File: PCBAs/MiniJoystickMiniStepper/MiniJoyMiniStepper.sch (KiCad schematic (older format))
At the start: 72 parts, among them J0 STEPPER_UNI_5P, J1 STEPPER_UNI_5P, J10 TH_0.1_1x1, J100 TH_0.1_1x1, J101 TH_0.1_1x1, J102 TH_0.1_1x1, J103 TH_0.1_1x1, J104 TH_0.1_1x1, J105 TH_0.1_1x1, J107 TH_0.1_1x1, J11 TH_0.1_1x1, J12 TH_0.1_1x1, J13 TH_0.1_1x1, J14 TH_0.1_1x1, J15 TH_0.1_1x1, J16 TH_0.1_1x1, J2 STEPPER_UNI_5P, J3 STEPPER_UNI_5P, J4 STEPPER_UNI_5P, J5 STEPPER_UNI_5P, J6 STEPPER_UNI_5P, J7 STEPPER_UNI_5P, J8 TH_0.1_1x1, J9 TH_0.1_1x1, U1 MCP3008T-I/SL, U10 ULN2803, U11 STM32F103C8T6_BLUE_PILL, U2 OLED_128x32_I2C, U3 CD74HC595, U4 CD74HC595, U5 CD74HC595, U6 CD74HC595, U7 ULN2803, U8 ULN2803, U9 ULN2803

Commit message: Updated daisy chain con, added motor power and xtra gnd
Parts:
- added JMOTOR_GND11, JMOTOR_GND3, J_MOTOR_POWER0, J_MOTOR_POWER1: TH_0.1_1x1, Liberry:single_0.1, symbol TH_0.1_1x1
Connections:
- wire segments 416 -> 423
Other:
- moved on the sheet: C1, J101, J102, J103, J104, J105, J107, J11, J12, J13, J14, J15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

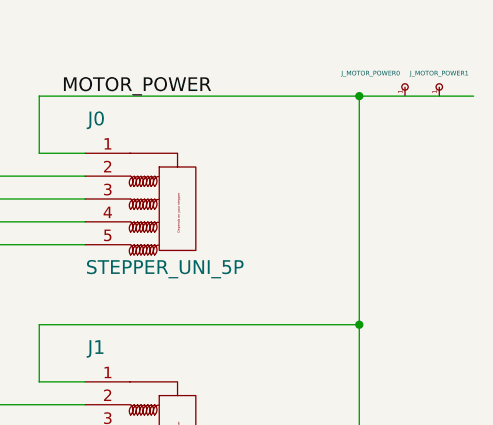
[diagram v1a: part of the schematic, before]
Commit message: Updated daisy chain. Added extra motor power pins for more current/heat disspation.
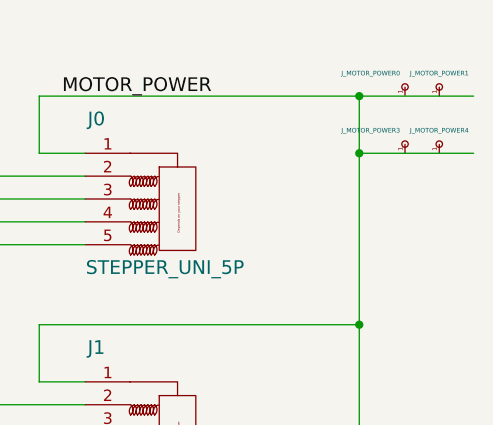
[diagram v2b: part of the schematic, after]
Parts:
- added J_MOTOR_POWER3, J_MOTOR_POWER4: TH_0.1_1x1, Liberry:single_0.1, symbol TH_0.1_1x1
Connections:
- wire segments 423 -> 424

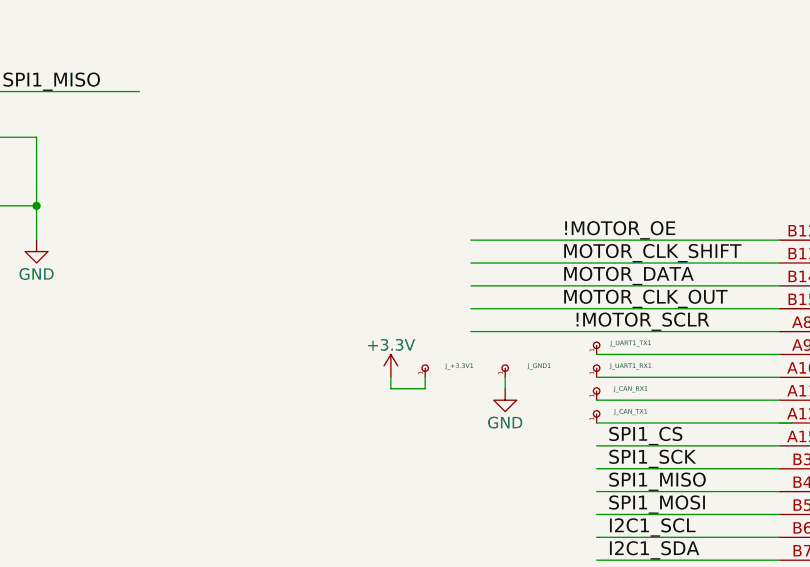
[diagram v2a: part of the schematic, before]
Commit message: Added FTDI to USB interface. PCB ready for routing
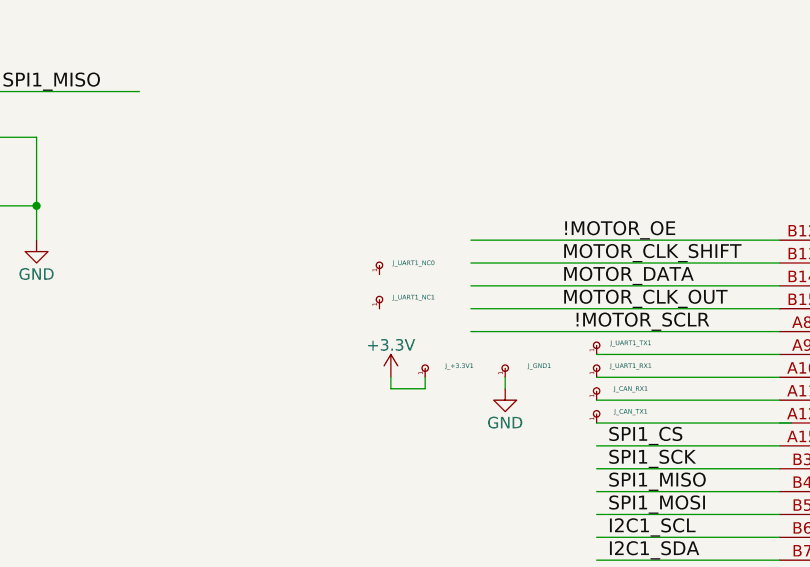
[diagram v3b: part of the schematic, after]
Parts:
- added J_UART1_NC0, J_UART1_NC1: TH_0.1_1x1, Liberry:single_0.1, symbol TH_0.1_1x1
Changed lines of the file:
@@
+	1    0    0    -1
+$EndComp
+$Comp
+L TH_0.1_1x1 J_UART1_NC0
+U 1 1 5A94D380
+P 7800 6400
+F 0 "J_UART1_NC0" H 7950 6450 20  0000 C CNN
+F 1 "TH_0.1_1x1" H 7800 6400 60  0001 C CNN
+F 2 "Liberry:single_0.1" H 7800 6400 60  0001 C CNN
+F 3 "" H 7800 6400 60  0001 C CNN
+	1    7800 6400
+	1    0    0    -1
+$EndComp
+$Comp
+L TH_0.1_1x1 J_UART1_NC1
+U 1 1 5A94D487
+P 7800 6550
+F 0 "J_UART1_NC1" H 7950 6600 20  0000 C CNN
+F 1 "TH_0.1_1x1" H 7800 6550 60  0001 C CNN
+F 2 "Liberry:single_0.1" H 7800 6550 60  0001 C CNN
+F 3 "" H 7800 6550 60  0001 C CNN
+	1    7800 6550
 	1    0    0    -1
 $EndComp

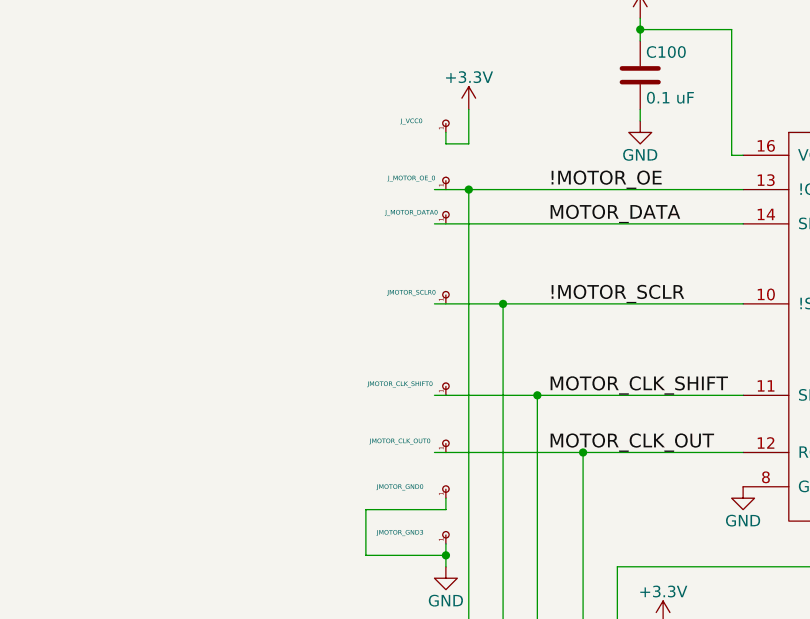
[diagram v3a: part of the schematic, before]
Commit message: Fixed PCB bug: Reconnected pads to nets
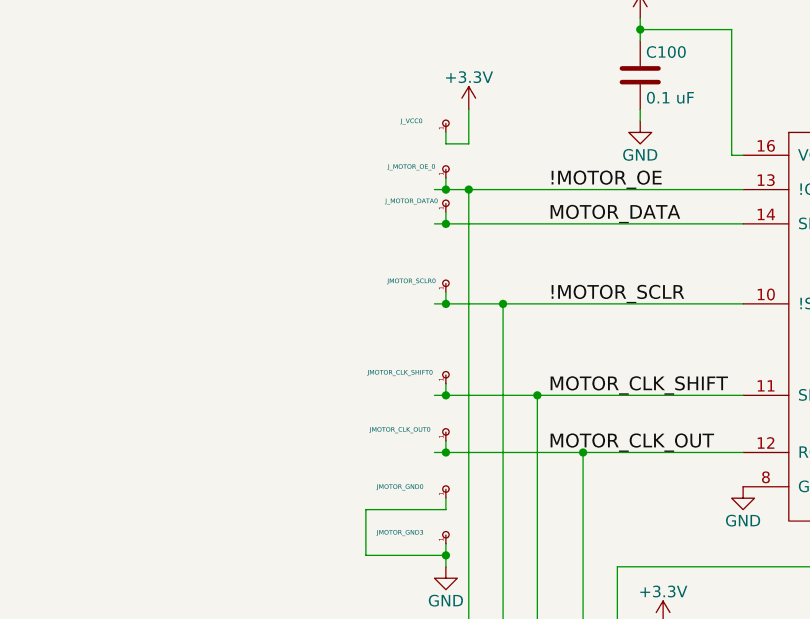
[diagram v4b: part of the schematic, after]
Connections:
- wire segments 424 -> 429
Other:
- moved on the sheet: JMOTOR_CLK_OUT0, JMOTOR_CLK_SHIFT0, JMOTOR_SCLR0, J_MOTOR_DATA0, J_MOTOR_OE_0
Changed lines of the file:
@@
 L TH_0.1_1x1 J_MOTOR_OE_0
 U 1 1 5A91B2F0
-P 15000 1400
-F 0 "J_MOTOR_OE_0" H 14850 1450 20  0000 C CNN
-F 1 "TH_0.1_1x1" H 15000 1400 60  0001 C CNN
-F 2 "Liberry:single_0.1" H 15000 1400 60  0001 C CNN
-F 3 "" H 15000 1400 60  0001 C CNN
-	1    15000 1400
+P 15000 1350
+F 0 "J_MOTOR_OE_0" H 14850 1400 20  0000 C CNN
+F 1 "TH_0.1_1x1" H 15000 1350 60  0001 C CNN
+F 2 "Liberry:single_0.1" H 15000 1350 60  0001 C CNN
+F 3 "" H 15000 1350 60  0001 C CNN
+	1    15000 1350
 	1    0    0    -1
 $EndComp
@@
 L TH_0.1_1x1 J_MOTOR_DATA0
 U 1 1 5A91C126
-P 15000 1550
-F 0 "J_MOTOR_DATA0" H 14850 1600 20  0000 C CNN
-F 1 "TH_0.1_1x1" H 15000 1550 60  0001 C CNN
-F 2 "Liberry:single_0.1" H 15000 1550 60  0001 C CNN
-F 3 "" H 15000 1550 60  0001 C CNN
-	1    15000 1550
+P 15000 1500
+F 0 "J_MOTOR_DATA0" H 14850 1550 20  0000 C CNN
+F 1 "TH_0.1_1x1" H 15000 1500 60  0001 C CNN
+F 2 "Liberry:single_0.1" H 15000 1500 60  0001 C CNN
+F 3 "" H 15000 1500 60  0001 C CNN
+	1    15000 1500
 	1    0    0    -1
 $EndComp
@@
 L TH_0.1_1x1 JMOTOR_SCLR0
 U 1 1 5A91C1E4
-P 15000 1900
-F 0 "JMOTOR_SCLR0" H 14850 1950 20  0000 C CNN
-F 1 "TH_0.1_1x1" H 15000 1900 60  0001 C CNN
-F 2 "Liberry:single_0.1" H 15000 1900 60  0001 C CNN
-F 3 "" H 15000 1900 60  0001 C CNN
-	1    15000 1900
+P 15000 1850
+F 0 "JMOTOR_SCLR0" H 14850 1900 20  0000 C CNN
+F 1 "TH_0.1_1x1" H 15000 1850 60  0001 C CNN
+F 2 "Liberry:single_0.1" H 15000 1850 60  0001 C CNN
+F 3 "" H 15000 1850 60  0001 C CNN
+	1    15000 1850
 	1    0    0    -1
 $EndComp
@@
 L TH_0.1_1x1 JMOTOR_CLK_SHIFT0
 U 1 1 5A91C2A9
-P 15000 2300
-F 0 "JMOTOR_CLK_SHIFT0" H 14800 2350 20  0000 C CNN
-F 1 "TH_0.1_1x1" H 15000 2300 60  0001 C CNN
-F 2 "Liberry:single_0.1" H 15000 2300 60  0001 C CNN
-F 3 "" H 15000 2300 60  0001 C CNN
-	1    15000 2300
+P 15000 2250
+F 0 "JMOTOR_CLK_SHIFT0" H 14800 2300 20  0000 C CNN
+F 1 "TH_0.1_1x1" H 15000 2250 60  0001 C CNN
+F 2 "Liberry:single_0.1" H 15000 2250 60  0001 C CNN
+F 3 "" H 15000 2250 60  0001 C CNN
+	1    15000 2250
 	1    0    0    -1
 $EndComp
@@
 L TH_0.1_1x1 JMOTOR_CLK_OUT0
 U 1 1 5A91CDDD
-P 15000 2550
-F 0 "JMOTOR_CLK_OUT0" H 14800 2600 20  0000 C CNN
-F 1 "TH_0.1_1x1" H 15000 2550 60  0001 C CNN
-F 2 "Liberry:single_0.1" H 15000 2550 60  0001 C CNN
-F 3 "" H 15000 2550 60  0001 C CNN
-	1    15000 2550
+P 15000 2500
+F 0 "JMOTOR_CLK_OUT0" H 14800 2550 20  0000 C CNN
+F 1 "TH_0.1_1x1" H 15000 2500 60  0001 C CNN
+F 2 "Liberry:single_0.1" H 15000 2500 60  0001 C CNN
+F 3 "" H 15000 2500 60  0001 C CNN
+	1    15000 2500
 	1    0    0    -1
 $EndComp
@@
 	1    0    0    -1
 $EndComp
+Wire Wire Line
+	15000 2250 15000 2300
+Connection ~ 15000 2300
+Wire Wire Line
+	15000 1900 15000 1850
+Connection ~ 15000 1900
+Wire Wire Line
+	15000 2500 15000 2550
+Connection ~ 15000 2550
+Wire Wire Line
+	15000 1350 15000 1400
+Connection ~ 15000 1400
+Wire Wire Line
+	15000 1500 15000 1550
+Connection ~ 15000 1550
 $EndSCHEMATC

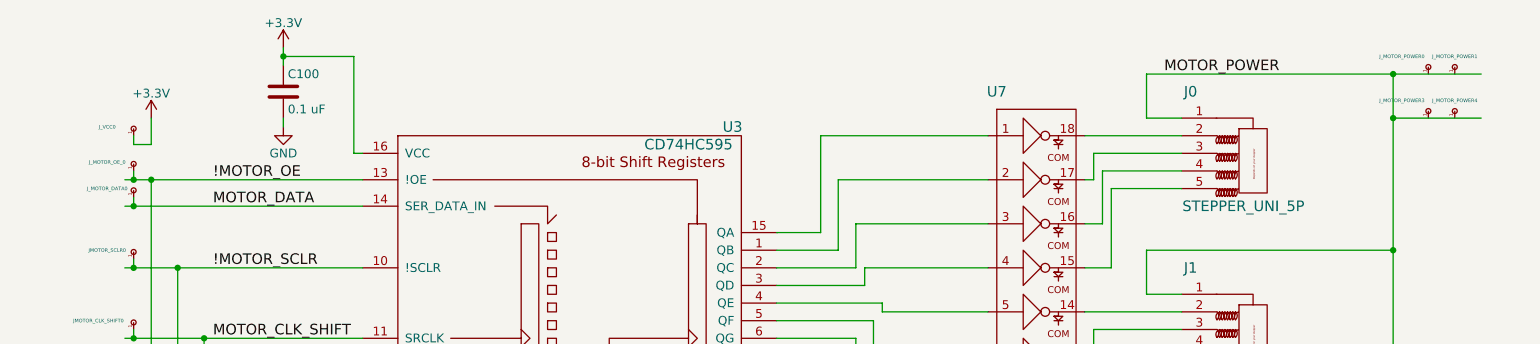
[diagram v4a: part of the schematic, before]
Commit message: PCB Midroute: Motor Driver + Shift Register routed.
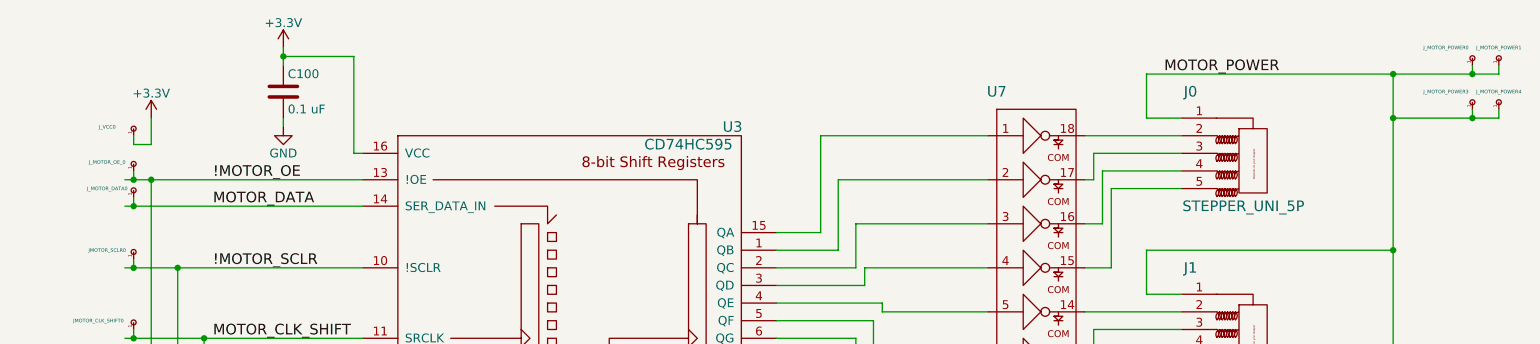
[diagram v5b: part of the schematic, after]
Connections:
- wire segments 429 -> 433
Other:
- moved on the sheet: J_MOTOR_POWER0, J_MOTOR_POWER1, J_MOTOR_POWER3, J_MOTOR_POWER4
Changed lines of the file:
@@
 	20750 1050 20750 800
-Wire Wire Line
-	20750 800  22650 800
 Wire Wire Line
 	22150 800  22150 10600
@@
 	14950 1900 16300 1900
 Wire Wire Line
-	16300 1550 14950 1550
+	14950 1550 16300 1550
 Wire Wire Line
 	14950 1400 16300 1400
@@
 L TH_0.1_1x1 J_MOTOR_POWER0
 U 1 1 5A942C87
-P 22350 800
-F 0 "J_MOTOR_POWER0" H 22200 900 20  0000 C CNN
-F 1 "TH_0.1_1x1" H 22350 800 60  0001 C CNN
-F 2 "Liberry:single_0.1" H 22350 800 60  0001 C CNN
-F 3 "" H 22350 800 60  0001 C CNN
-	1    22350 800
+P 22600 750
+F 0 "J_MOTOR_POWER0" H 22450 850 20  0000 C CNN
+F 1 "TH_0.1_1x1" H 22600 750 60  0001 C CNN
+F 2 "Liberry:single_0.1" H 22600 750 60  0001 C CNN
+F 3 "" H 22600 750 60  0001 C CNN
+	1    22600 750
 	1    0    0    -1
 $EndComp
@@
 L TH_0.1_1x1 J_MOTOR_POWER1
 U 1 1 5A943526
-P 22500 800
-F 0 "J_MOTOR_POWER1" H 22500 900 20  0000 C CNN
-F 1 "TH_0.1_1x1" H 22500 800 60  0001 C CNN
-F 2 "Liberry:single_0.1" H 22500 800 60  0001 C CNN
-F 3 "" H 22500 800 60  0001 C CNN
-	1    22500 800
+P 22750 750
+F 0 "J_MOTOR_POWER1" H 22750 850 20  0000 C CNN
+F 1 "TH_0.1_1x1" H 22750 750 60  0001 C CNN
+F 2 "Liberry:single_0.1" H 22750 750 60  0001 C CNN
+F 3 "" H 22750 750 60  0001 C CNN
+	1    22750 750
 	1    0    0    -1
 $EndComp
@@
 Connection ~ 15000 3000
 Wire Wire Line
-	22150 1050 22650 1050
+	22150 1050 22750 1050
 Connection ~ 22150 1050
 $Comp
 L TH_0.1_1x1 J_MOTOR_POWER3
 U 1 1 5A949643
-P 22350 1050
-F 0 "J_MOTOR_POWER3" H 22200 1150 20  0000 C CNN
-F 1 "TH_0.1_1x1" H 22350 1050 60  0001 C CNN
-F 2 "Liberry:single_0.1" H 22350 1050 60  0001 C CNN
-F 3 "" H 22350 1050 60  0001 C CNN
-	1    22350 1050
+P 22600 1000
+F 0 "J_MOTOR_POWER3" H 22450 1100 20  0000 C CNN
+F 1 "TH_0.1_1x1" H 22600 1000 60  0001 C CNN
+F 2 "Liberry:single_0.1" H 22600 1000 60  0001 C CNN
+F 3 "" H 22600 1000 60  0001 C CNN
+	1    22600 1000
 	1    0    0    -1
 $EndComp
@@
 L TH_0.1_1x1 J_MOTOR_POWER4
 U 1 1 5A949740
-P 22500 1050
-F 0 "J_MOTOR_POWER4" H 22500 1150 20  0000 C CNN
-F 1 "TH_0.1_1x1" H 22500 1050 60  0001 C CNN
-F 2 "Liberry:single_0.1" H 22500 1050 60  0001 C CNN
-F 3 "" H 22500 1050 60  0001 C CNN
-	1    22500 1050
+P 22750 1000
+F 0 "J_MOTOR_POWER4" H 22750 1100 20  0000 C CNN
+F 1 "TH_0.1_1x1" H 22750 1000 60  0001 C CNN
+F 2 "Liberry:single_0.1" H 22750 1000 60  0001 C CNN
+F 3 "" H 22750 1000 60  0001 C CNN
+	1    22750 1000
 	1    0    0    -1
 $EndComp
@@
 	15000 1500 15000 1550
 Connection ~ 15000 1550
+Wire Wire Line
+	22600 800  22600 750
+Connection ~ 22600 800
+Wire Wire Line
+	22750 800  22750 750
+Wire Wire Line
+	22600 1000 22600 1050
+Connection ~ 22600 1050
+Wire Wire Line
+	22750 1050 22750 1000
+Wire Wire Line
+	20750 800  22750 800
 $EndSCHEMATC

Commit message: PCB First route complete. Files not ready for fab.
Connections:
- net labels removed: VCC
- wire segments 433 -> 505

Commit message: Sch: Fixed power net bug to joysticks. VCC->3.3V
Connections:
- wire segments 505 -> 432
